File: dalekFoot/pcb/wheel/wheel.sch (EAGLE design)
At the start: 78 parts, among them IC1 LM1117MP-3.3, IC2 LM1117MP-3.3, IC3 LM1117MP-3.3, IC4 4051D, IC5 4051D, IC6 LM1117MP-3.3, K1 12X12-TACTILE, K2 12X12-TACTILE, K3 12X12-TACTILE, K4 12X12-TACTILE, K5 12X12-TACTILE, U1 TB6612FNG(O,C,8,EL, U2 SS8050-SOT-23, U3 SS8050-SOT-23, U4 SS8050-SOT-23, U5 TB6612FNG(O,C,8,EL, U6 TB6612FNG(O,C,8,EL

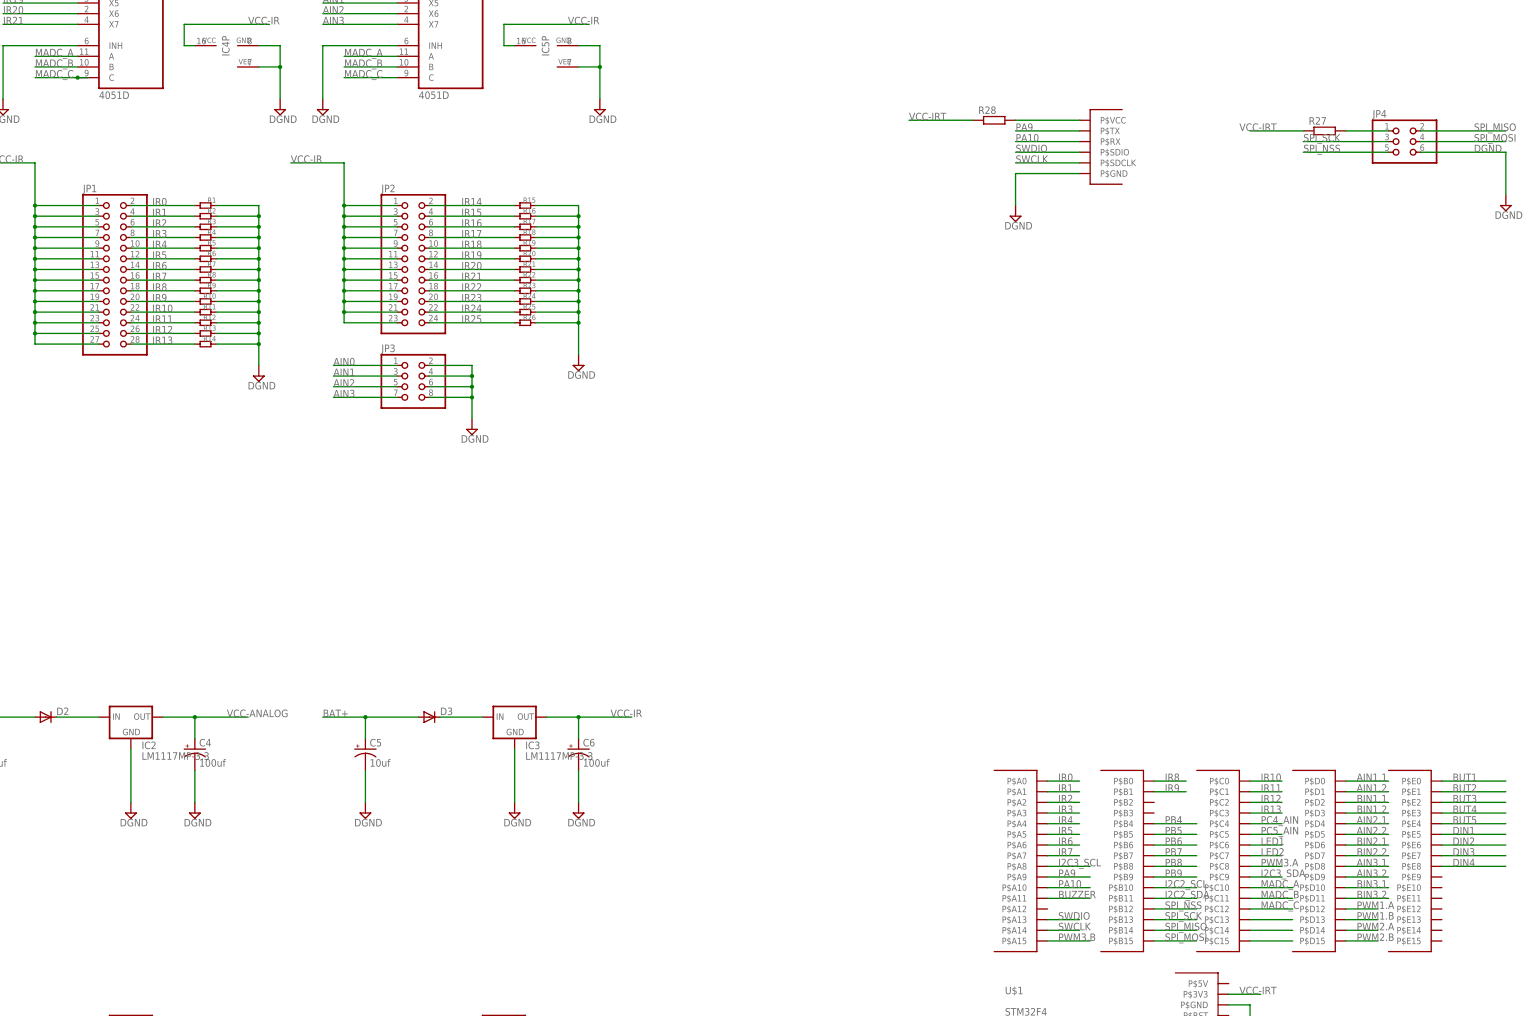
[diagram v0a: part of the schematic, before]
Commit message: bugfix: remove unused pin
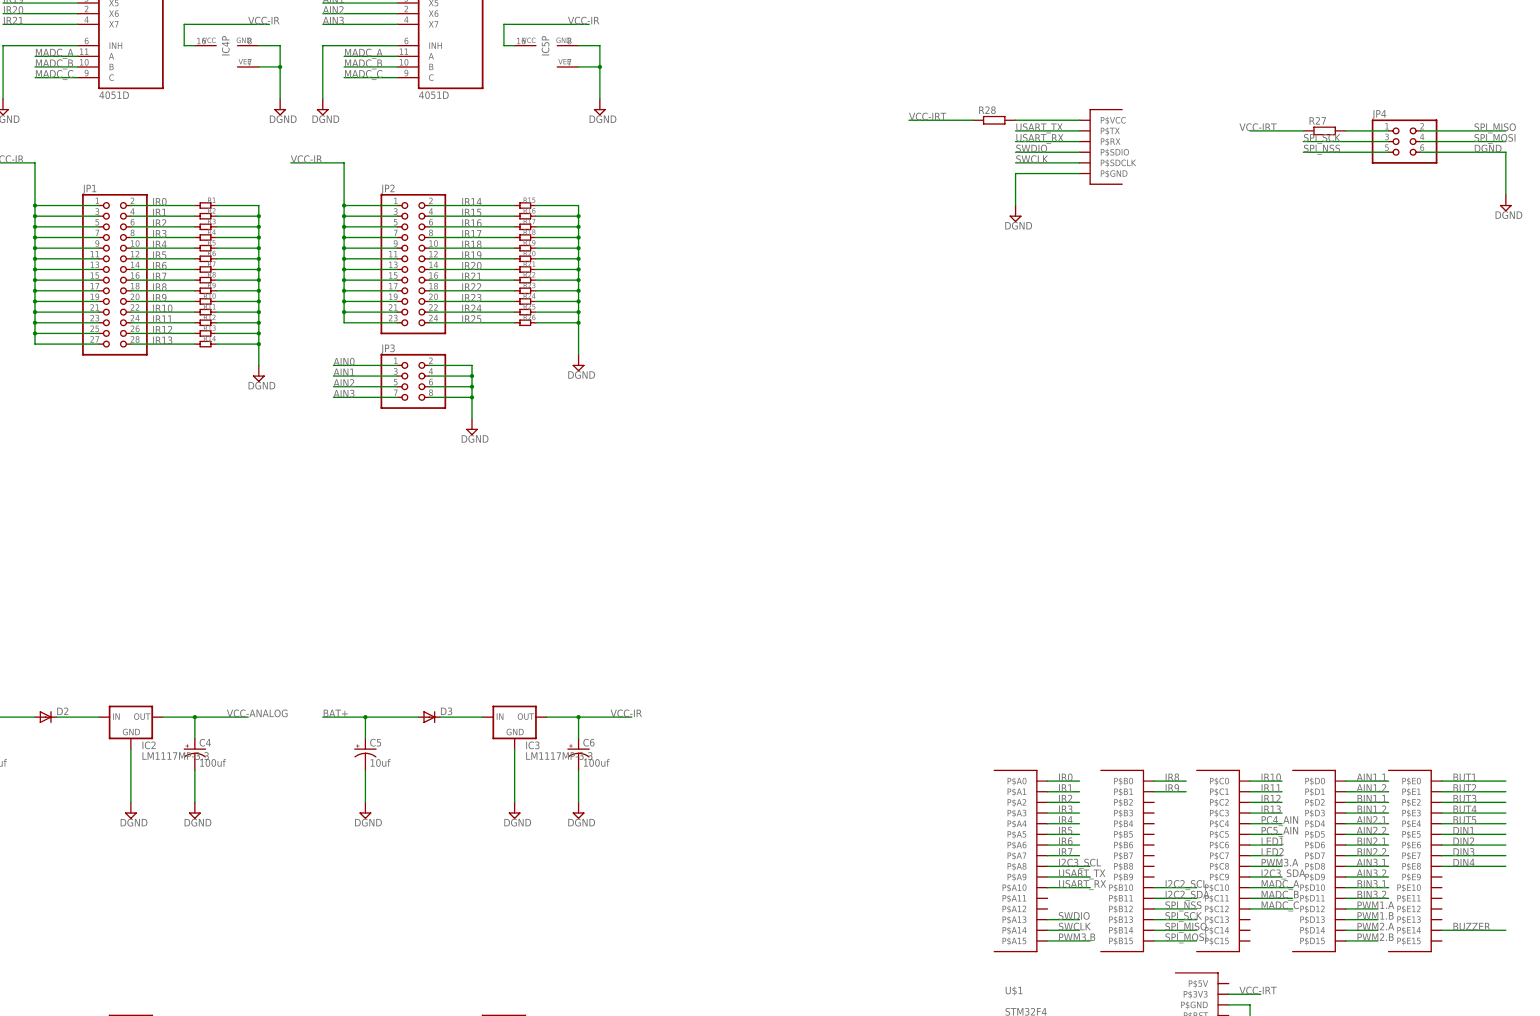
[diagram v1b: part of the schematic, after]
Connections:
- net PA10 renamed USART_RX
- net PA9 renamed USART_TX
- removed net N$28: U$1.P$C13
- removed net N$29: U$1.P$C14
- removed net N$30: U$1.P$C15
- removed net PB4: U$1.P$B4
- removed net PB5: U$1.P$B5
- removed net PB6: U$1.P$B6
- removed net PB7: U$1.P$B7
- removed net PB8: U$1.P$B8
- removed net PB9: U$1.P$B9
- net BUZZER: now also U$1.P$E14; no longer U$1.P$A11
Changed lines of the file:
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@@
 <label x="40.64" y="271.78" size="1.778" layer="95"/>
 <pinref part="IC4" gate="A" pin="C"/>
-<wire x1="50.8" y1="271.78" x2="53.34" y2="271.78" width="0.1524" layer="91"/>
-<junction x="50.8" y="271.78"/>
 </segment>
 <segment>
@@
 <wire x1="289.56" y1="261.62" x2="274.32" y2="261.62" width="0.1524" layer="91"/>
 <pinref part="R28" gate="G$1" pin="2"/>
-</segment>
-</net>
-<net name="PA9" class="0">
-<segment>
-<pinref part="J1" gate="G$1" pin="P$TX"/>
-<wire x1="274.32" y1="259.08" x2="289.56" y2="259.08" width="0.1524" layer="91"/>
-<label x="274.32" y="259.08" size="1.778" layer="95"/>
-</segment>
-<segment>
-<pinref part="U$1" gate="G$1" pin="P$A9"/>
-<wire x1="281.94" y1="81.28" x2="292.1" y2="81.28" width="0.1524" layer="91"/>
-<label x="284.48" y="81.28" size="1.778" layer="95"/>
-</segment>
-</net>
-<net name="PA10" class="0">
-<segment>
-<pinref part="J1" gate="G$1" pin="P$RX"/>
-<wire x1="289.56" y1="256.54" x2="274.32" y2="256.54" width="0.1524" layer="91"/>
-<label x="274.32" y="256.54" size="1.778" layer="95"/>
-</segment>
-<segment>
-<pinref part="U$1" gate="G$1" pin="P$A10"/>
-<wire x1="281.94" y1="78.74" x2="292.1" y2="78.74" width="0.1524" layer="91"/>
-<label x="284.48" y="78.74" size="1.778" layer="95"/>
-</segment>
-</net>
-<net name="PB8" class="0">
-<segment>
-<pinref part="U$1" gate="G$1" pin="P$B8"/>
-<wire x1="307.34" y1="83.82" x2="317.5" y2="83.82" width="0.1524" layer="91"/>
-<label x="309.88" y="83.82" size="1.778" layer="95"/>
-</segment>
-</net>
-<net name="PB9" class="0">
-<segment>
-<pinref part="U$1" gate="G$1" pin="P$B9"/>
-<wire x1="307.34" y1="81.28" x2="317.5" y2="81.28" width="0.1524" layer="91"/>
-<label x="309.88" y="81.28" size="1.778" layer="95"/>
-</segment>
-</net>
-<net name="PB4" class="0">
-<segment>
-<pinref part="U$1" gate="G$1" pin="P$B4"/>
-<wire x1="307.34" y1="93.98" x2="317.5" y2="93.98" width="0.1524" layer="91"/>
-<label x="309.88" y="93.98" size="1.778" layer="95"/>
-</segment>
-</net>
-<net name="PB5" class="0">
-<segment>
-<pinref part="U$1" gate="G$1" pin="P$B5"/>
-<wire x1="307.34" y1="91.44" x2="317.5" y2="91.44" width="0.1524" layer="91"/>
-<label x="309.88" y="91.44" size="1.778" layer="95"/>
-</segment>
-</net>
-<net name="PB6" class="0">
-<segment>
-<pinref part="U$1" gate="G$1" pin="P$B6"/>
-<wire x1="307.34" y1="88.9" x2="317.5" y2="88.9" width="0.1524" layer="91"/>
-<label x="309.88" y="88.9" size="1.778" layer="95"/>
-</segment>
-</net>
-<net name="PB7" class="0">
-<segment>
-<pinref part="U$1" gate="G$1" pin="P$B7"/>
-<wire x1="307.34" y1="86.36" x2="317.5" y2="86.36" width="0.1524" layer="91"/>
-<label x="309.88" y="86.36" size="1.778" layer="95"/>
 </segment>
 </net>
@@
 </segment>
 </net>
-<net name="N$28" class="0">
-<segment>
-<pinref part="U$1" gate="G$1" pin="P$C13"/>
-<wire x1="330.2" y1="71.12" x2="340.36" y2="71.12" width="0.1524" layer="91"/>
-</segment>
-</net>
-<net name="N$29" class="0">
-<segment>
-<pinref part="U$1" gate="G$1" pin="P$C14"/>
-<wire x1="330.2" y1="68.58" x2="340.36" y2="68.58" width="0.1524" layer="91"/>
-</segment>
-</net>
-<net name="N$30" class="0">
-<segment>
-<pinref part="U$1" gate="G$1" pin="P$C15"/>
-<wire x1="330.2" y1="66.04" x2="340.36" y2="66.04" width="0.1524" layer="91"/>
-</segment>
-</net>
 <net name="BUT1" class="0">
 <segment>
@@
 <net name="BUZZER" class="0">
 <segment>
-<pinref part="U$1" gate="G$1" pin="P$A11"/>
-<wire x1="281.94" y1="76.2" x2="292.1" y2="76.2" width="0.1524" layer="91"/>
-<label x="284.48" y="76.2" size="1.778" layer="95"/>
-</segment>
-<segment>
 <pinref part="R29" gate="G$1" pin="P$1"/>
 <wire x1="20.32" y1="431.8" x2="12.7" y2="431.8" width="0.1524" layer="91"/>
 <label x="15.24" y="431.8" size="1.778" layer="95"/>
+</segment>
+<segment>
+<pinref part="U$1" gate="G$1" pin="P$E14"/>
+<wire x1="375.92" y1="68.58" x2="391.16" y2="68.58" width="0.1524" layer="91"/>
+<label x="378.46" y="68.58" size="1.778" layer="95"/>
 </segment>
 </net>
@@
 </segment>
 </net>
+<net name="USART_TX" class="0">
+<segment>
+<pinref part="U$1" gate="G$1" pin="P$A9"/>
+<wire x1="281.94" y1="81.28" x2="292.1" y2="81.28" width="0.1524" layer="91"/>
+<label x="284.48" y="81.28" size="1.778" layer="95"/>
+</segment>
+<segment>
+<pinref part="J1" gate="G$1" pin="P$TX"/>
+<wire x1="274.32" y1="259.08" x2="289.56" y2="259.08" width="0.1524" layer="91"/>
+<label x="274.32" y="259.08" size="1.778" layer="95"/>
+</segment>
+</net>
+<net name="USART_RX" class="0">
+<segment>
+<pinref part="U$1" gate="G$1" pin="P$A10"/>
+<wire x1="281.94" y1="78.74" x2="292.1" y2="78.74" width="0.1524" layer="91"/>
+<label x="284.48" y="78.74" size="1.778" layer="95"/>
+</segment>
+<segment>
+<pinref part="J1" gate="G$1" pin="P$RX"/>
+<wire x1="289.56" y1="256.54" x2="274.32" y2="256.54" width="0.1524" layer="91"/>
+<label x="274.32" y="256.54" size="1.778" layer="95"/>
+</segment>
+</net>

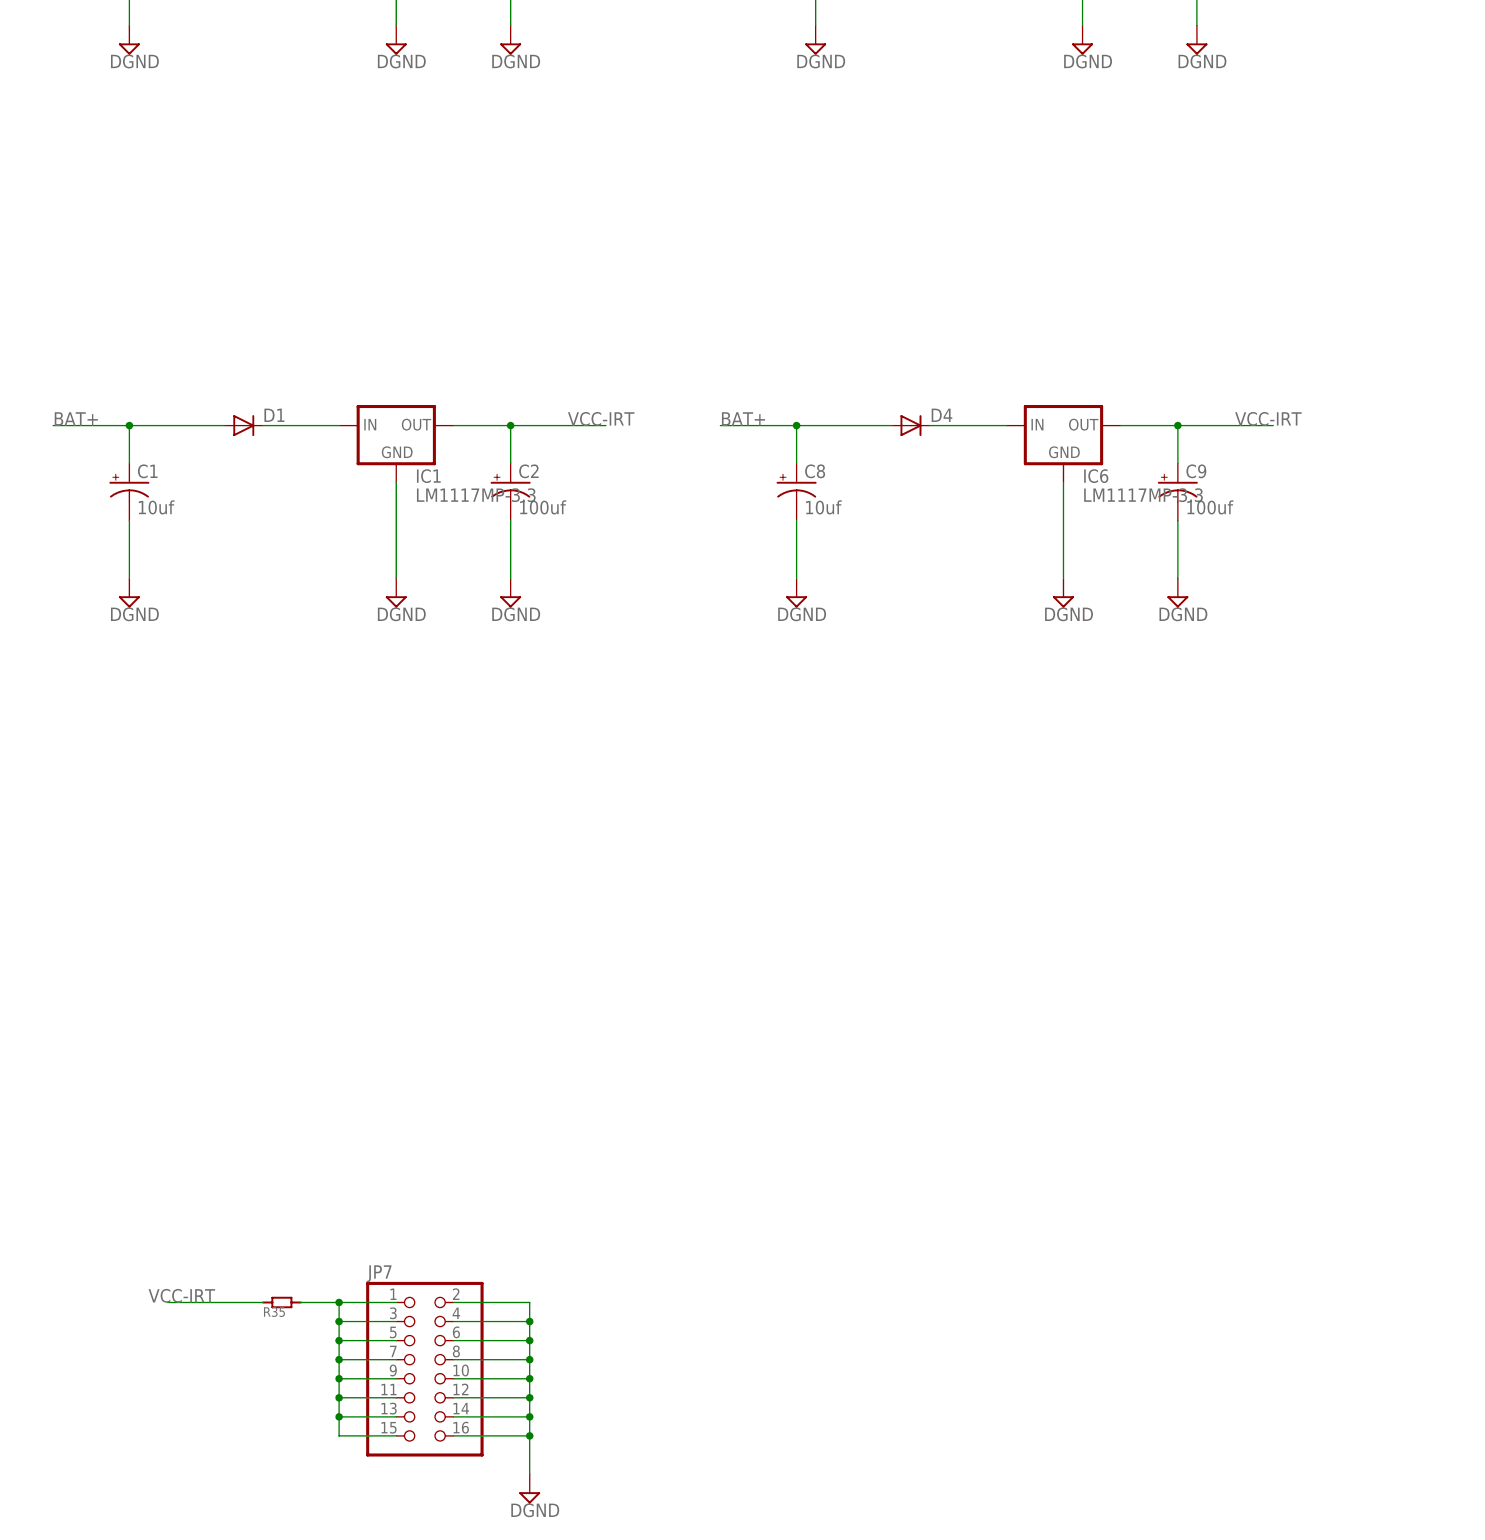
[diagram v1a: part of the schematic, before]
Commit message: bugfix: add missing battery connector
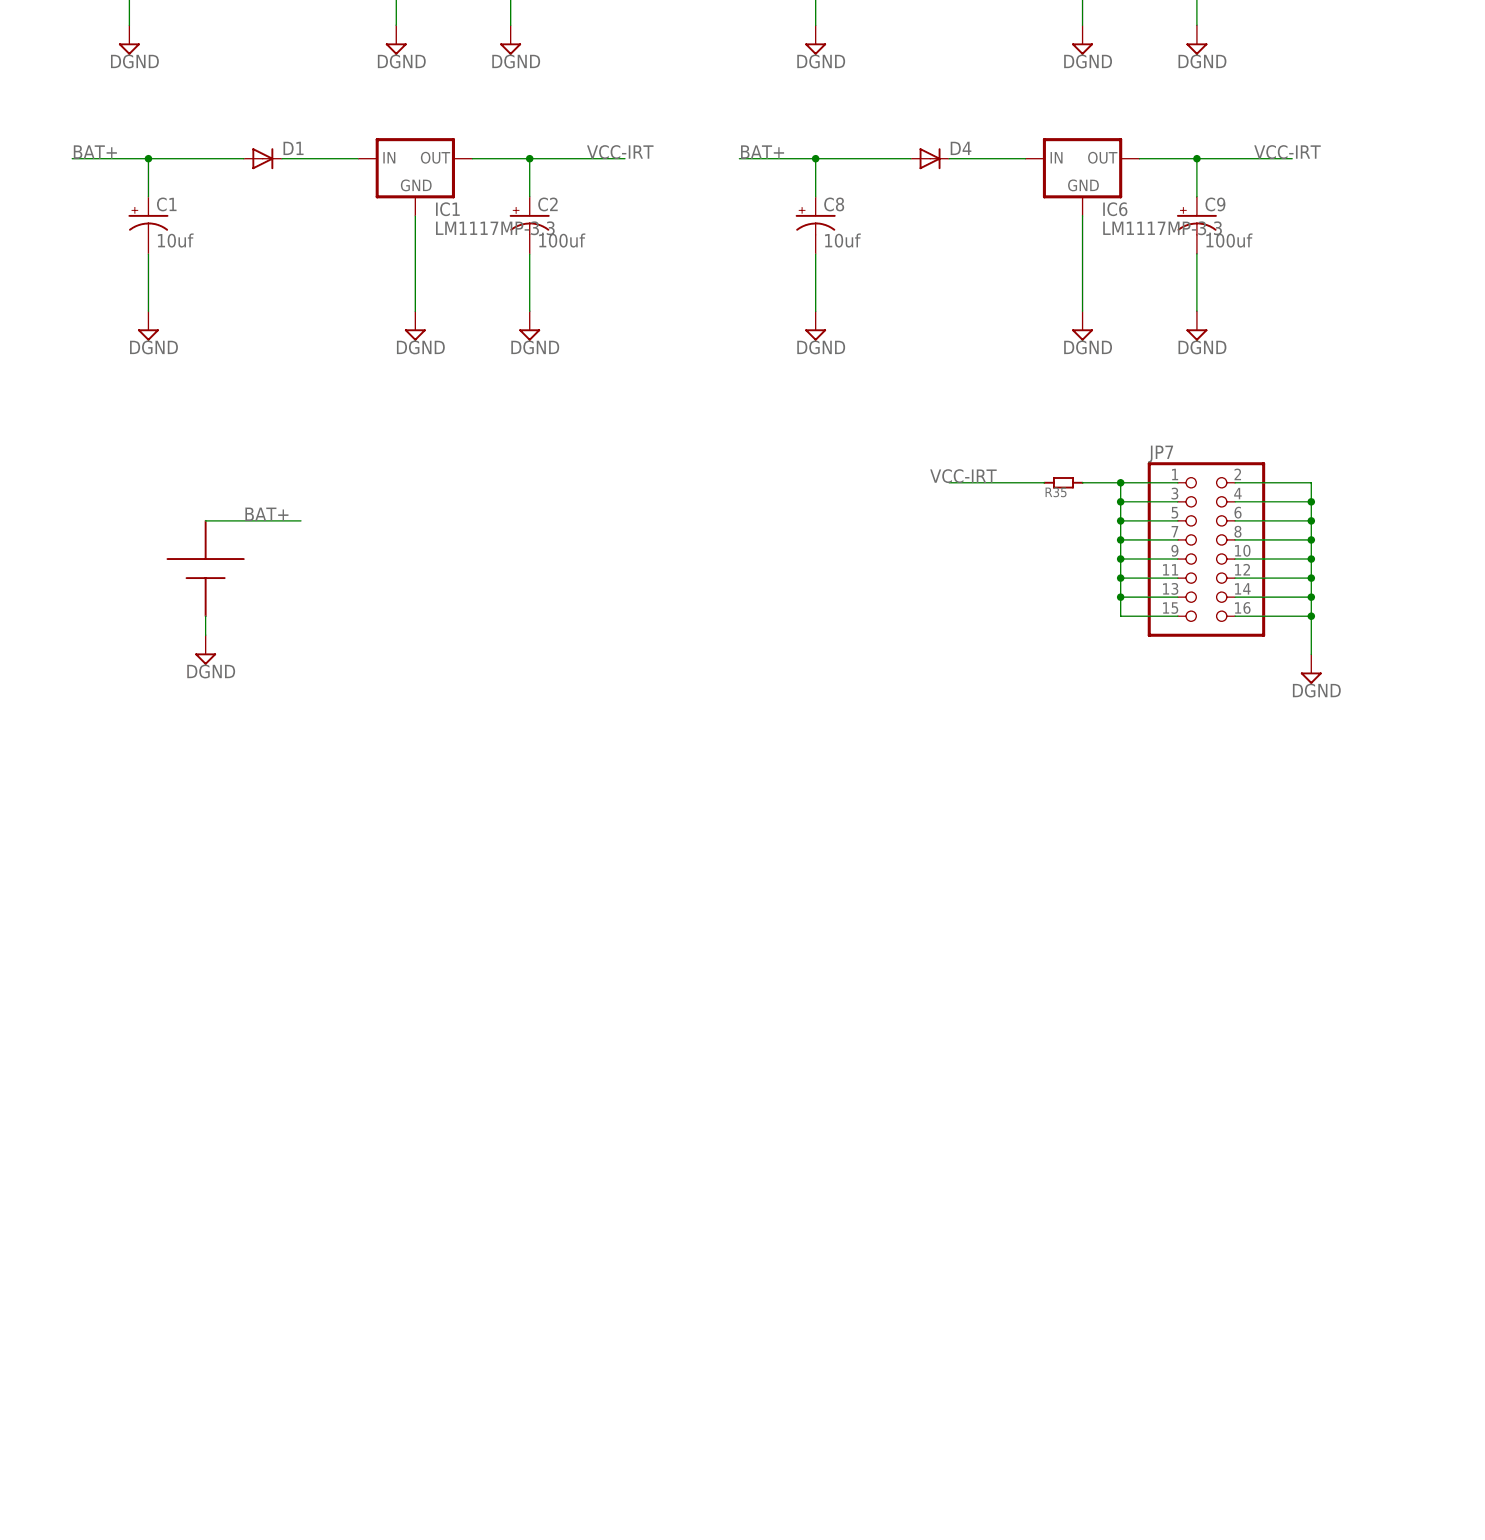
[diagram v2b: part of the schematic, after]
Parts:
- added U$2: BATTERY-10A, hqc:BATTERY-10A
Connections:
- net BAT+: now also U$2.P$POS
- net DGND: now also U$2.P$NEG
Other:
- moved on the sheet: C1, C2, C8, C9, D1, D4, IC1, IC6, JP7, R35
